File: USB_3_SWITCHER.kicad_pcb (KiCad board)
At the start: 4 copper layers, 122 x 56 mm, 304 parts, among them J1 Jack-DC, J2 Wuerth_USB3_B_Receptable_6922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, J3 Wuerth_USB3_B_Receptable_6922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, J4 Wuerth_USB3_Receptible_692122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, J5 Wuerth_USB3_Receptible_692122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, J6 Wuerth_USB3_Receptible_692122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, J7 Wuerth_USB3_Receptible_692122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, J8 Conn_01x16_Pin, J9 Conn_01x04_Pin, Q1 NTJD4401NT1G, Q2 NTJD4401NT1G, Q3 NTJD4401NT1G, Q4 NTJD4401NT1G, Q5 NTJD4401NT1G, Q6 NTJD4401NT1G, Q7 NTJD4401NT1G, Q8 NTJD4401NT1G, Q9 NTJD4401NT1G, SW1 SW_Omron_B3FS, SW2 SW_Omron_B3FS, U1 AT24CS04-SSHM, U10 LM66100DCK, U11 TPD6E05U06RVZ, U12 MAX8586, U13 TPD6E05U06RVZ, U14 MAX8586, U15 TPD6E05U06RVZ, U16 MAX8586, U17 TPD6E05U06RVZ, U18 MAX8586, U19 TPD6E05U06RVZ, U2 TUSB8043A, U20 74LVC1G08, U21 74LVC1G08, U22 LM397, U23 74LVC1G17, U24 74LVC2G74, U25 74LVC1G17, U26 74LVC1G32, U27 74LVC1G08, U28 ISO1540, U29 74LVC1G32, U3 TS3USB30EDGSR, U30 74LVC1G08, U4 CBTL02043A, U5 LM66100DCK, U6 LMR33640ADDA, U7 LMR33640ADDA, U8 LM66100DCK, U9 TPD6E05U06RVZ, Y1 24MHz 20ppm

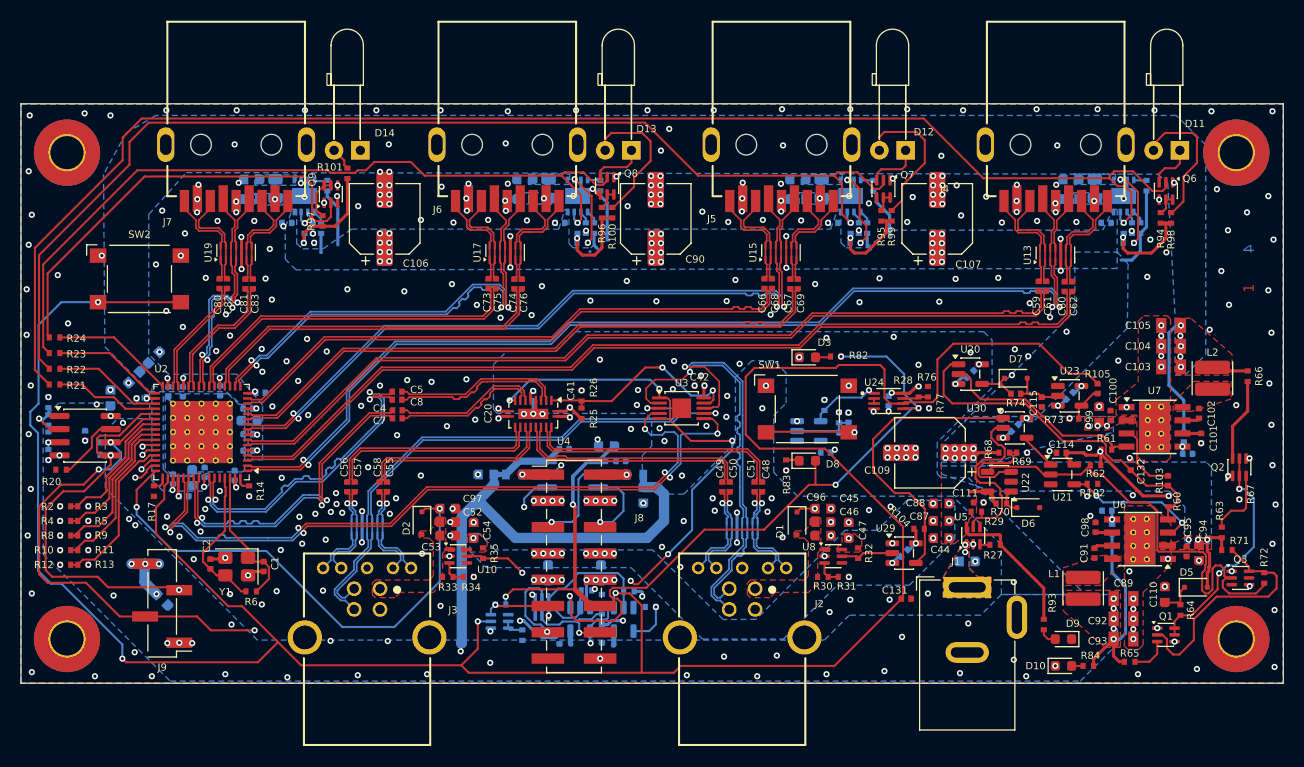
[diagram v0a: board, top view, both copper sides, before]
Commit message: Power In Circuitry extended for more current
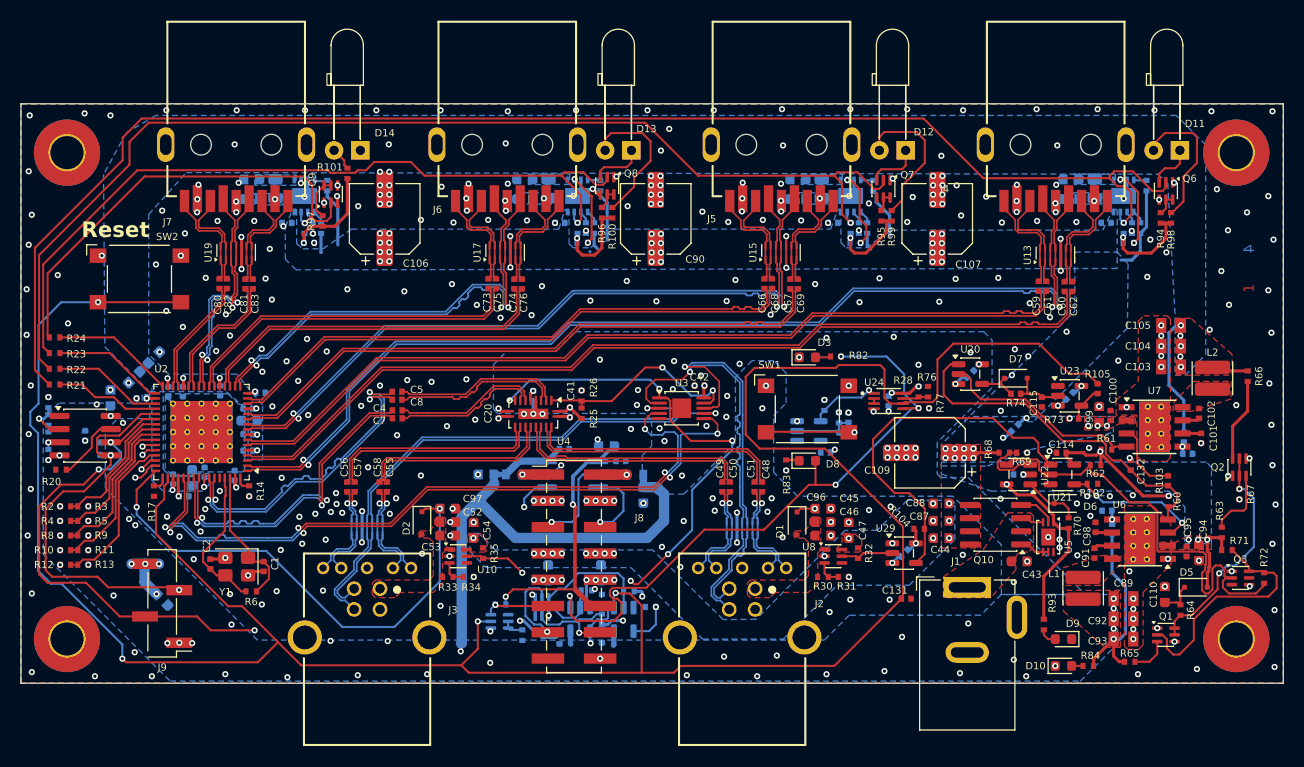
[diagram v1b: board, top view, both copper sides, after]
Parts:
- removed R27: 1k, 00_Resistor:Res_0402
- removed R29: 10k, 00_Resistor:Res_0402
- removed U30: 74LVC1G08, Package_TO_SOT_SMD:SOT-23-5
- added Q10: Si4162DY, Package_SO:SOIC-8_3.9x4.9mm_P1.27mm, F.Cu at (235.2, 143.2)
- C111: moved to B.Cu
- C43: moved to F.Cu
- U5: value LM66100DCK -> LTC4359-DCB; footprint Package_TO_SOT_SMD:SOT-363_SC-70-6 -> Package_DFN_QFN:DFN-6-1EP_3x2mm_P0.5mm_EP1.65x1.35mm
- moved U5 7.25 mm to (240.3, 144.4), turned to -90 degrees
- moved R70 6.77 mm to (242.2, 143.0), turned to -90 degrees
- moved C43 5.03 mm to (237.5, 146.7)
- moved C111 4.70 mm to (237.4, 138.3)
- moved D6 3.62 mm to (241.9, 141.1)
- moved U22 1.98 mm to (237.4, 138.3)
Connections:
- U21 pad 1: Net-(U21-Pad1) -> Net-(R104-Pad2)
- U5 pad 1: VIN -> +5V
- U5 pad 2: GND -> Net-(Q10-G)
- U5 pad 3: Net-(U5-~{CE}) -> VIN
- U5 pad 4: unconnected-(U5-NC-Pad4) -> VIN
- U5 pad 5: /POWER_SUPPLY/U5_ST -> VIN
- U5 pad 6: +5V -> GND
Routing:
- net /POWER_SUPPLY/U5_ST: track 18.1 -> 0.00 mm
- net Net-(R104-Pad2): track 28.6 -> 35.6 mm
- net VIN: track 0.00 -> 5.20 mm, vias 2 -> 0
- net Net-(Q10-G): track 0.00 -> 3.59 mm
- net Net-(U21-Pad1): track 3.56 -> 0.00 mm
- net Net-(U22-+): track 9.30 -> 6.20 mm
- net /POWER_SEQUENCING/VREF: track 2.48 -> 5.57 mm
- net /POWER_SEQUENCING/VIN_PGOOD: track 44.2 -> 43.1 mm
- net +5V: track 56.1 -> 57.1 mm, vias 51 -> 52
- net Net-(U5-~{CE}): track 0.90 -> 0.00 mm
- net GND: vias 431 -> 438
- removed copper zone on B.Cu, net VIN
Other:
- board text added: "Reset"

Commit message: Restored
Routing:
- net /DOWNSTREAM_CONNECTORS1/USB_DS_SSRX_N: track 9.41 -> 11.1 mm
- net /DOWNSTREAM_CONNECTORS1/USB_DS_SSRX_P: track 9.52 -> 11.0 mm
- net /DOWNSTREAM_CONNECTORS2/USB_DS_SSRX_P: track 9.38 -> 10.8 mm
- net /DOWNSTREAM_CONNECTORS2/USB_DS_D_N: track 42.6 -> 43.6 mm
- net /DOWNSTREAM_CONNECTORS2/USB_DS_SSTX_P: track 9.72 -> 10.4 mm
- net /DOWNSTREAM_CONNECTORS/USB_DS_SSRX_C_P: track 83.9 -> 84.4 mm
- net /DOWNSTREAM_CONNECTORS/USB_DS_SSRX_C_N: track 83.8 -> 84.4 mm
- net /DOWNSTREAM_CONNECTORS2/USB_DS_SSRX_C_P: track 33.1 -> 32.5 mm
- net /DOWNSTREAM_CONNECTORS2/USB_DS_SSRX_C_N: track 33.1 -> 32.5 mm
- net GND: vias 438 -> 448
